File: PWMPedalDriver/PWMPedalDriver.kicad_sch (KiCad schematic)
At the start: 13 parts, among them U1 TLV172IDCK, U2 TLV172IDCK, U3 TLV172IDCK

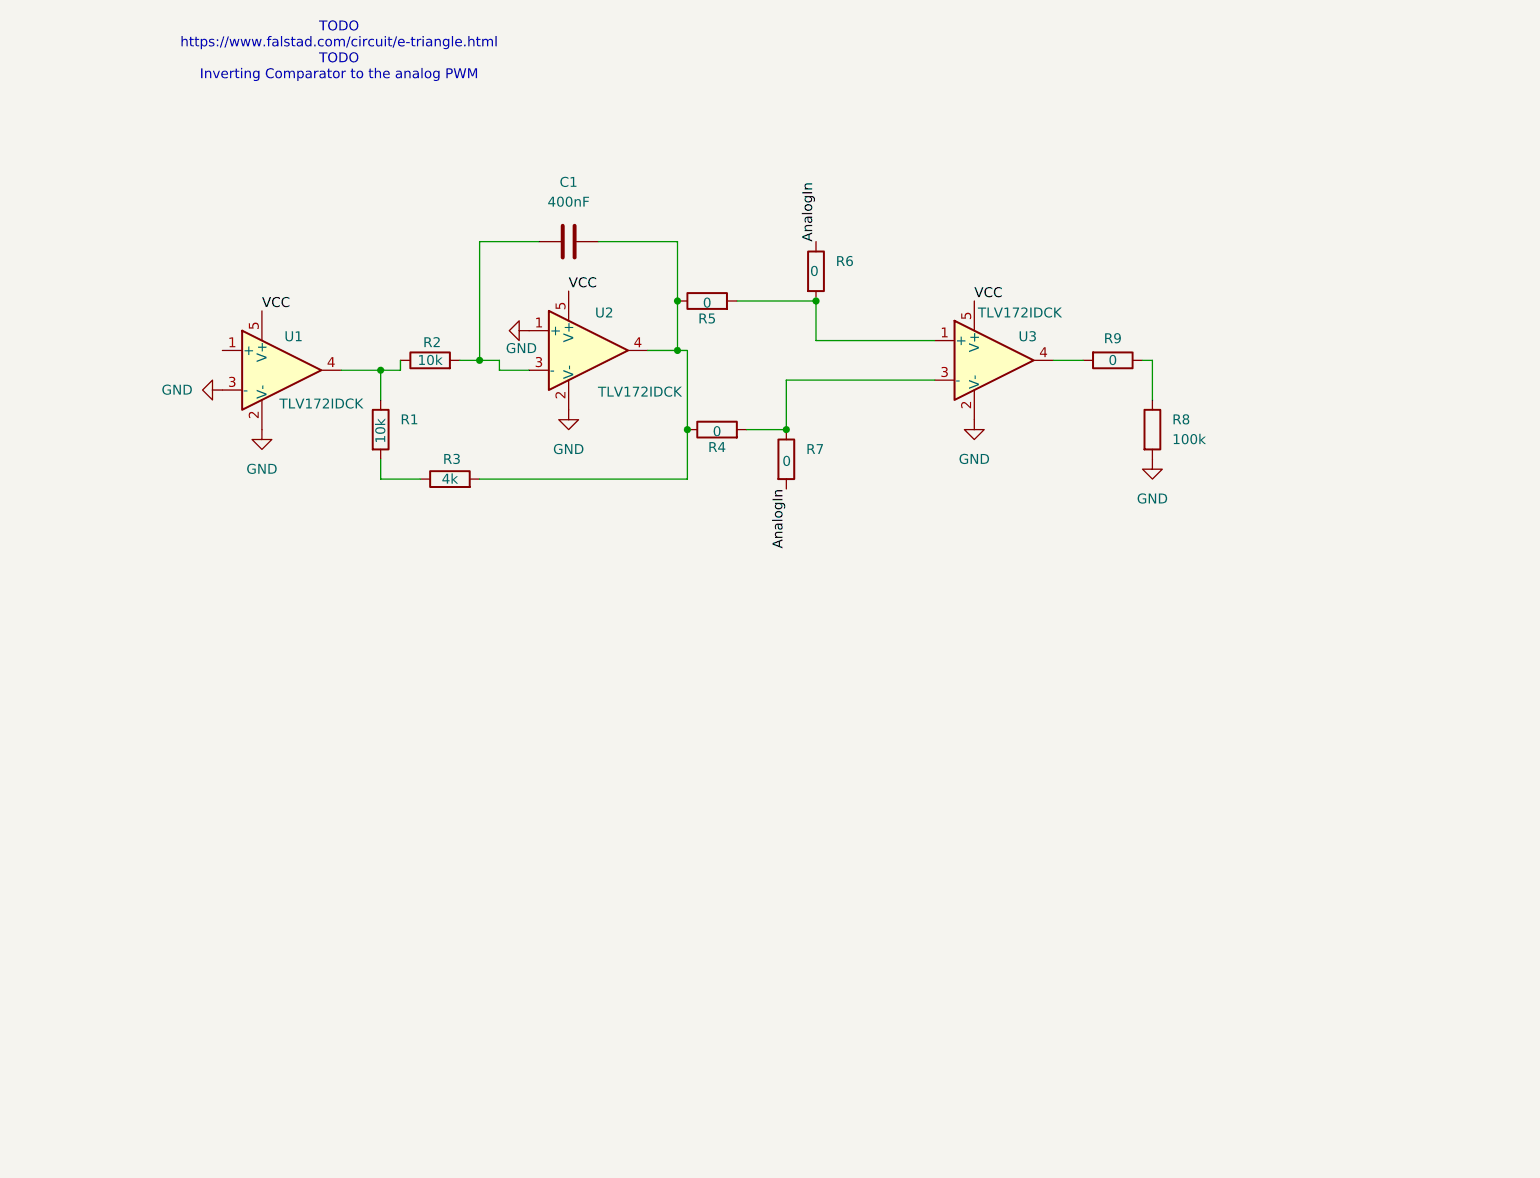
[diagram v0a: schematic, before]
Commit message: Simulated Triangle -> PWM Driver.
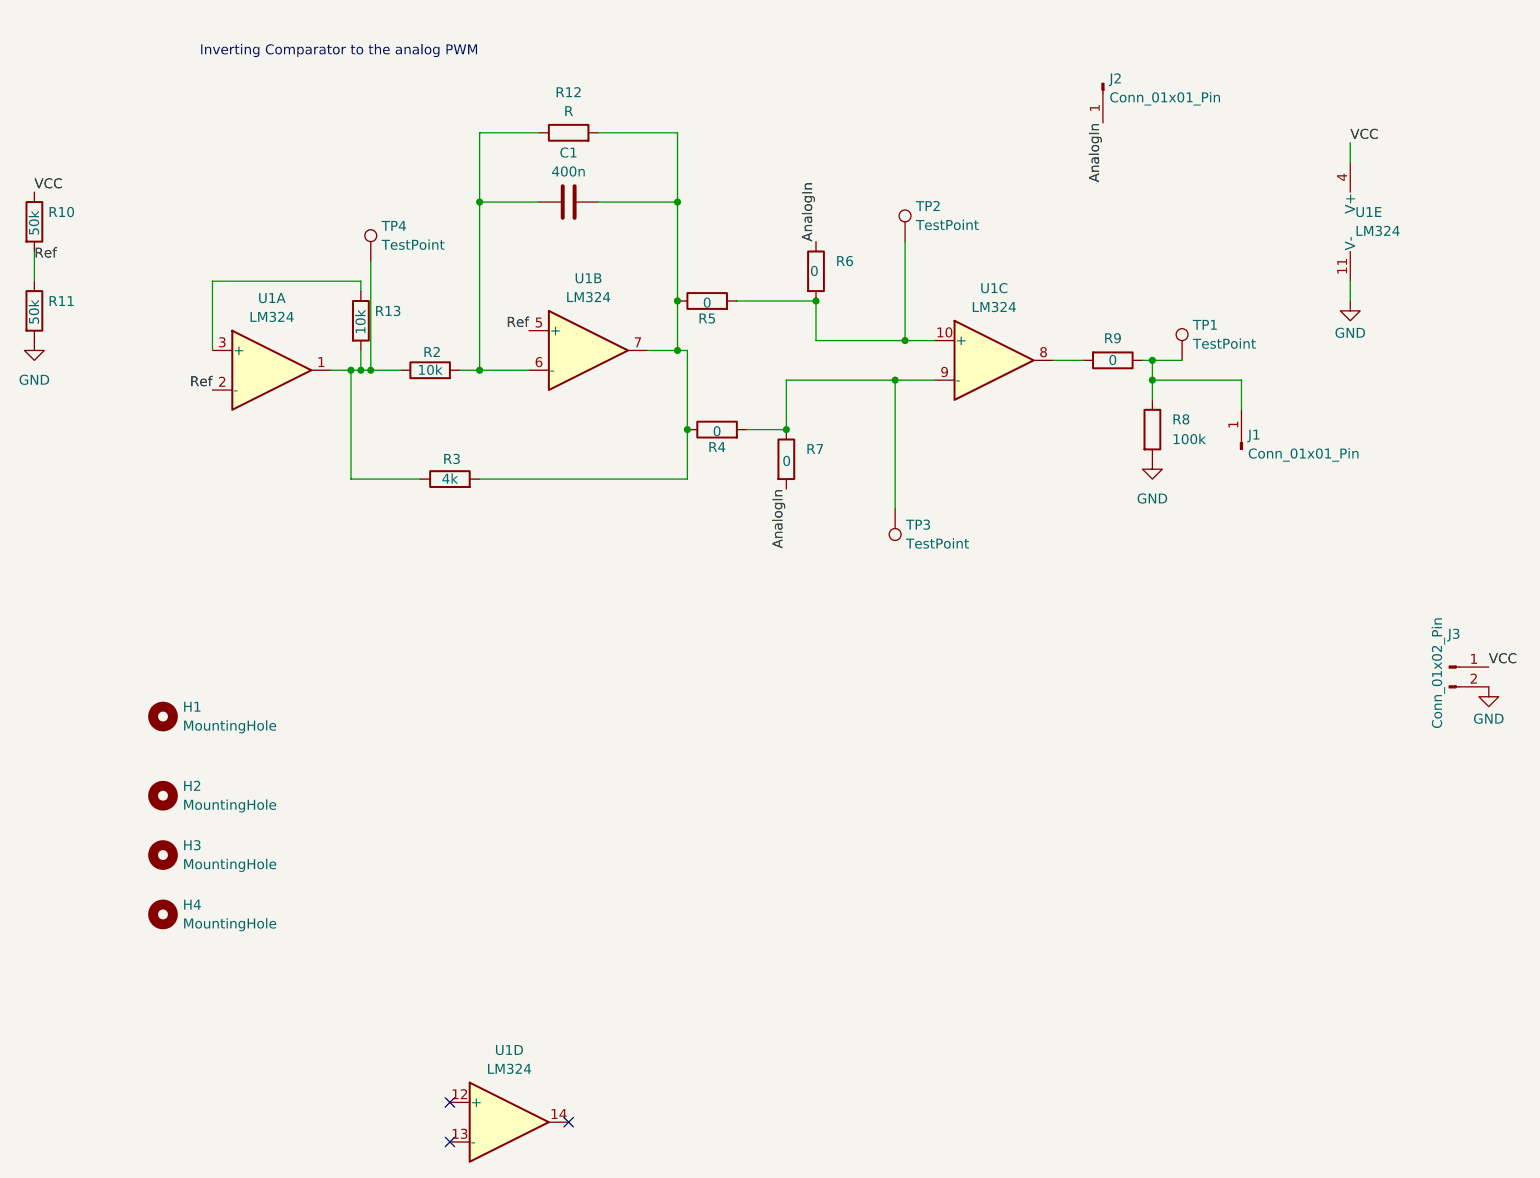
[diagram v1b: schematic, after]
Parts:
- removed R1: 10k, symbol Device:R
- removed U1, U2, U3: TLV172IDCK, Package_TO_SOT_SMD:SOT-353_SC-70-5, symbol Amplifier_Operational:TLV172IDCK
- added H1, H2, H3, H4: MountingHole, MountingHole:MountingHole_3.2mm_M3, symbol Mechanical:MountingHole
- added J1, J2: Conn_01x01_Pin, Connector_PinHeader_2.54mm:PinHeader_1x01_P2.54mm_Vertical, symbol Connector:Conn_01x01_Pin
- added J3: Conn_01x02_Pin, Connector_PinHeader_2.54mm:PinHeader_1x02_P2.54mm_Vertical, symbol Connector:Conn_01x02_Pin
- added R10, R11: 50k, Resistor_SMD:R_0402_1005Metric_Pad0.72x0.64mm_HandSolder, symbol Device:R
- added R12: R, Resistor_SMD:R_0402_1005Metric_Pad0.72x0.64mm_HandSolder, symbol Device:R
- added R13: 10k, Resistor_SMD:R_0402_1005Metric_Pad0.72x0.64mm_HandSolder, symbol Device:R
- added TP1, TP2, TP3, TP4: TestPoint, TestPoint:TestPoint_Loop_D2.60mm_Drill1.4mm_Beaded, symbol Connector:TestPoint
- added U1: LM324, Package_SO:SOIC-14_3.9x8.7mm_P1.27mm, symbol Amplifier_Operational:LM324
- C1: value 400nF -> 400n; footprint (none) -> Capacitor_SMD:C_0402_1005Metric_Pad0.74x0.62mm_HandSolder
- R2, R3, R4, R5, R6, R7, R8, R9: footprint (none) -> Resistor_SMD:R_0402_1005Metric_Pad0.72x0.64mm_HandSolder
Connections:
- net AnalogIn: now also J2.1 (Pin_1)
- net GND: now also J3.2 (Pin_2), R11.2, U1.11 (V-)
- net VCC: now also J3.1 (Pin_1), R10.1, U1.4 (V+)
- net at R2.1: now also R3.1, R13.2, TP4.1, U1.1
- net at C1.2, R3.2, R4.1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: now also R12.2, U1.7
- net at R4.2, R7.1: now also TP3.1, U1.9 (-)
- net at R5.2, R6.2: now also TP2.1, U1.10 (+)
- net at C1.1, R2.2: now also R12.1, U1.6 (-)
- net at R9.2: now also U1.8
- net at R8.1, R9.1: now also J1.1 (Pin_1), TP1.1
- new net: R13.1, U1.3 (+)
- new net Ref: R10.2, R11.1, U1.2 (-), U1.5 (+)
- no-connect marks 0 -> 3
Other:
- note added: "Inverting Comparator to the analog PWM"
- note removed: "TODO https://www.falstad.com/circuit/e-triangle.html TODO Inverting Comparator to the analog PWM"
- moved on the sheet: C1, R2

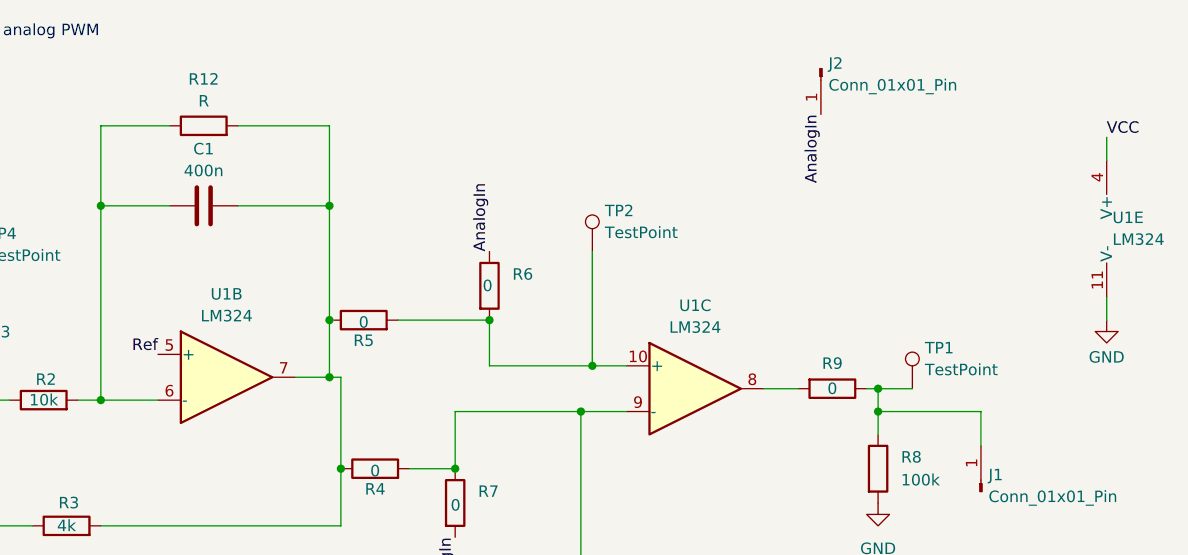
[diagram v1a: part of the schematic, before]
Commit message: First pass placement
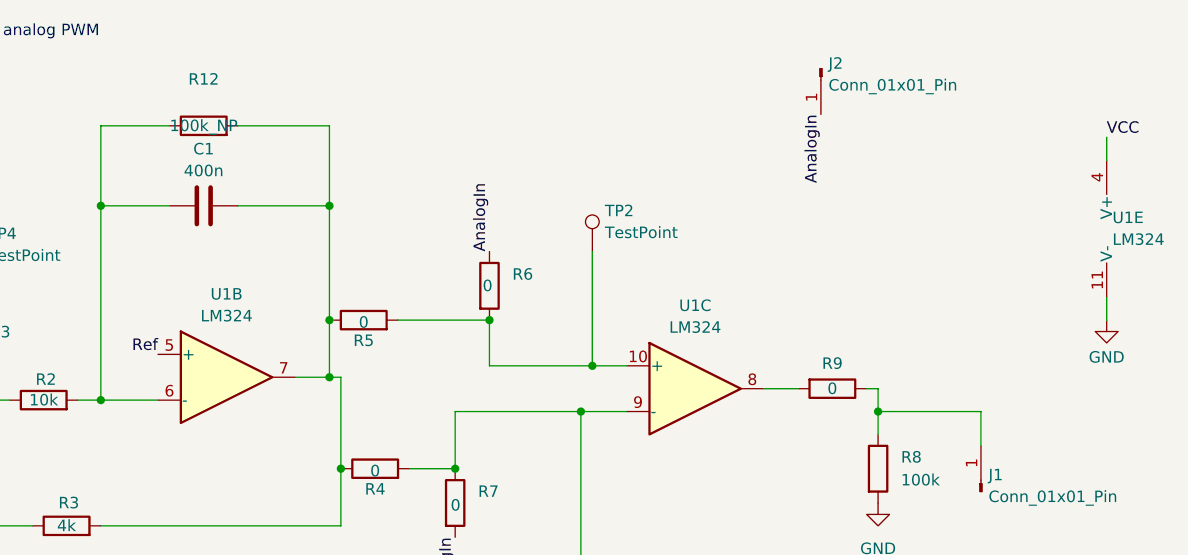
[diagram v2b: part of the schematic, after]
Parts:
- removed TP1: TestPoint, TestPoint:TestPoint_Loop_D2.60mm_Drill1.4mm_Beaded, symbol Connector:TestPoint
- R12: value R -> 100k_NP
- TP2, TP3, TP4: footprint TestPoint:TestPoint_Loop_D2.60mm_Drill1.4mm_Beaded -> TestPoint:TestPoint_Loop_D2.60mm_Drill0.9mm_Beaded
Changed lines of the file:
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@@
-	)
-	(junction
-		(at 227.33 60.96)
-		(diameter 0)
-		(color 0 0 0 0)
 	)
 	(junction
@@
 		(pts
 			(xy 227.33 60.96) (xy 227.33 63.5)
-		)
-		(stroke
-			(width 0)
-			(type default)
-		)
-	)
-	(wire
-		(pts
-			(xy 227.33 60.96) (xy 231.14 60.96)
 		)
 		(stroke
@@
 			)
 		)
-		(property "Footprint" "TestPoint:TestPoint_Loop_D2.60mm_Drill1.4mm_Beaded"
+		(property "Footprint" "TestPoint:TestPoint_Loop_D2.60mm_Drill0.9mm_Beaded"
 			(at 200.66 45.72 0)
 			(effects
@@
 		(on_board yes)
 		(dnp no)
-		(fields_autoplaced yes)
 		(property "Reference" "R12"
 			(at 152.4 26.5895 90)
@@
 			)
 		)
-		(property "Value" "R"
-			(at 152.4 29.0138 90)
+		(property "Value" "100k_NP"
+			(at 152.4 31.75 90)
 			(effects
 				(font
@@
 			)
 		)
-		(property "Footprint" "TestPoint:TestPoint_Loop_D2.60mm_Drill1.4mm_Beaded"
+		(property "Footprint" "TestPoint:TestPoint_Loop_D2.60mm_Drill0.9mm_Beaded"
 			(at 132.08 48.26 0)
 			(effects
@@
 	(symbol
 		(lib_id "Connector:TestPoint")
-		(at 231.14 60.96 0)
-		(unit 1)
-		(exclude_from_sim no)
-		(in_bom yes)
-		(on_board yes)
-		(dnp no)
-		(fields_autoplaced yes)
-		(property "Reference" "TP1"
-			(at 232.537 56.4458 0)
-			(effects
-				(font
-					(size 1.27 1.27)
-				)
-				(justify left)
-			)
-		)
-		(property "Value" "TestPoint"
-			(at 232.537 58.8701 0)
-			(effects
-				(font
-					(size 1.27 1.27)
-				)
-				(justify left)
-			)
-		)
-		(property "Footprint" "TestPoint:TestPoint_Loop_D2.60mm_Drill1.4mm_Beaded"
-			(at 236.22 60.96 0)
-			(effects
-				(font
-					(size 1.27 1.27)
-				)
-				(hide yes)
-			)
-		)
-		(property "Datasheet" "~"
-			(at 236.22 60.96 0)
-			(effects
-				(font
-					(size 1.27 1.27)
-				)
-				(hide yes)
-			)
-		)
-		(property "Description" "test point"
-			(at 231.14 60.96 0)
-			(effects
-				(font
-					(size 1.27 1.27)
-				)
-				(hide yes)
-			)
-		)
-		(pin "1"
-		)
-		(instances
-			(project ""
-				(path "/ca3f4581-2760-476b-ae38-fbfd5da505cf"
-					(reference "TP1")
-					(unit 1)
-				)
-			)
-		)
-	)
-	(symbol
-		(lib_id "Connector:TestPoint")
 		(at 194.31 80.01 180)
 		(unit 1)
@@
 			)
 		)
-		(property "Footprint" "TestPoint:TestPoint_Loop_D2.60mm_Drill1.4mm_Beaded"
+		(property "Footprint" "TestPoint:TestPoint_Loop_D2.60mm_Drill0.9mm_Beaded"
 			(at 189.23 80.01 0)
 			(effects

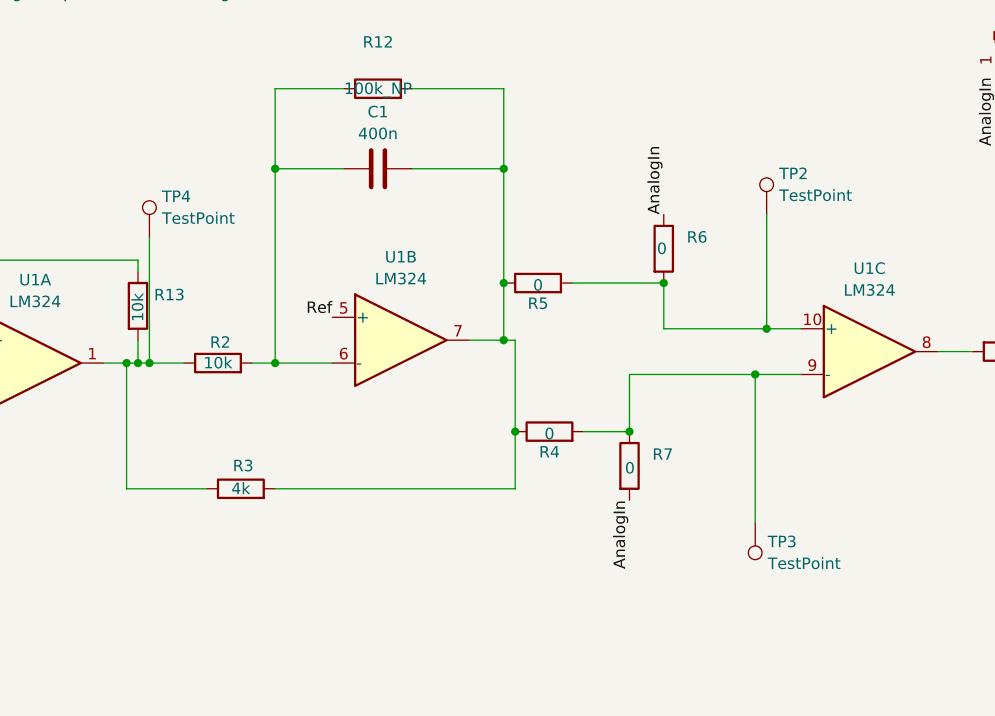
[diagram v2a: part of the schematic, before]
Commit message: Potential Routing / Placement for PWM
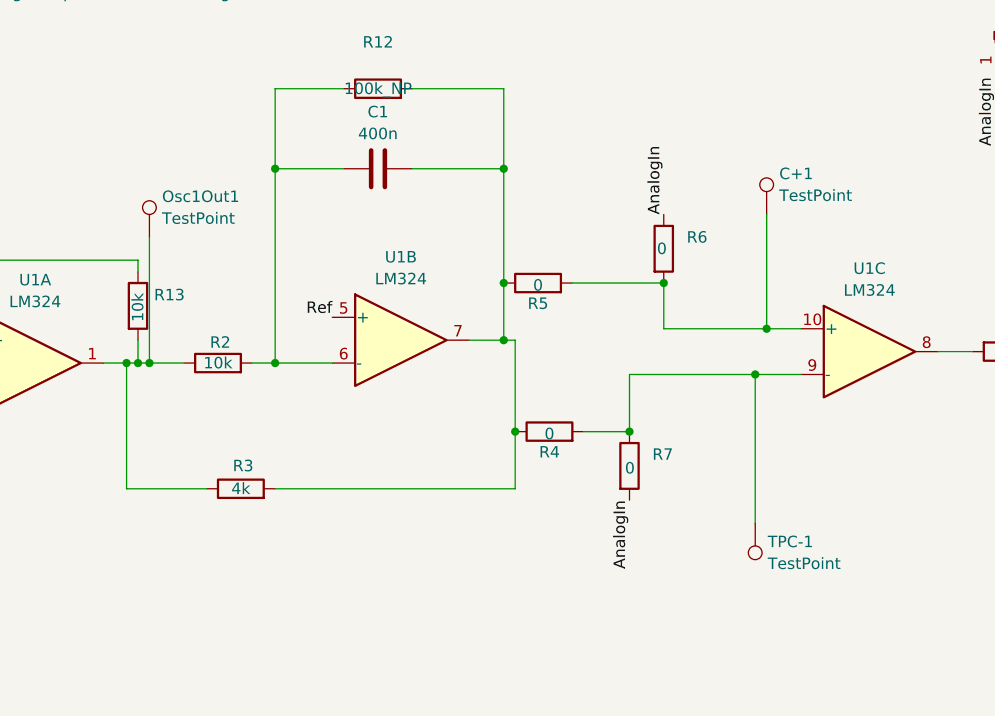
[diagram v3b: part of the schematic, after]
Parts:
- renumbered TP2 to C+1, TP4 to Osc1Out1, TP3 to TPC-1
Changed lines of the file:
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@@
 		(dnp no)
 		(fields_autoplaced yes)
-		(property "Reference" "TP2"
+		(property "Reference" "C+1"
 			(at 196.977 41.2058 0)
 			(effects
@@
 			(project "PWMPedalDriver"
 				(path "/ca3f4581-2760-476b-ae38-fbfd5da505cf"
-					(reference "TP2")
+					(reference "C+1")
 					(unit 1)
 				)
@@
 		(dnp no)
 		(fields_autoplaced yes)
-		(property "Reference" "TP4"
+		(property "Reference" "Osc1Out1"
 			(at 128.397 43.7458 0)
 			(effects
@@
 			(project "PWMPedalDriver"
 				(path "/ca3f4581-2760-476b-ae38-fbfd5da505cf"
-					(reference "TP4")
+					(reference "Osc1Out1")
 					(unit 1)
 				)
@@
 		(dnp no)
 		(fields_autoplaced yes)
-		(property "Reference" "TP3"
+		(property "Reference" "TPC-1"
 			(at 195.707 82.0998 0)
 			(effects
@@
 			(project "PWMPedalDriver"
 				(path "/ca3f4581-2760-476b-ae38-fbfd5da505cf"
-					(reference "TP3")
-					(unit 1)
-				)
+					(reference "TPC-1")
+					(unit 1)
+				)

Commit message: Shipped Board
Shipped out the Analog -> PWM driver
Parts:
- removed H1, H2: MountingHole, MountingHole:MountingHole_3.2mm_M3, symbol Mechanical:MountingHole
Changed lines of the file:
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@@
-	)
-	(symbol
-		(lib_id "Mechanical:MountingHole")
-		(at 100.33 116.84 0)
-		(unit 1)
-		(exclude_from_sim yes)
-		(in_bom no)
-		(on_board yes)
-		(dnp no)
-		(fields_autoplaced yes)
-		(property "Reference" "H2"
-			(at 102.87 115.6278 0)
-			(effects
-				(font
-					(size 1.27 1.27)
-				)
-				(justify left)
-			)
-		)
-		(property "Value" "MountingHole"
-			(at 102.87 118.0521 0)
-			(effects
-				(font
-					(size 1.27 1.27)
-				)
-				(justify left)
-			)
-		)
-		(property "Footprint" "MountingHole:MountingHole_3.2mm_M3"
-			(at 100.33 116.84 0)
-			(effects
-				(font
-					(size 1.27 1.27)
-				)
-				(hide yes)
-			)
-		)
-		(property "Datasheet" "~"
-			(at 100.33 116.84 0)
-			(effects
-				(font
-					(size 1.27 1.27)
-				)
-				(hide yes)
-			)
-		)
-		(property "Description" "Mounting Hole without connection"
-			(at 100.33 116.84 0)
-			(effects
-				(font
-					(size 1.27 1.27)
-				)
-				(hide yes)
-			)
-		)
-		(instances
-			(project "PWMPedalDriver"
-				(path "/ca3f4581-2760-476b-ae38-fbfd5da505cf"
-					(reference "H2")
-					(unit 1)
-				)
-			)
-		)
 	)
 	(symbol
@@
 					(unit 1)
 				)
-			)
-		)
-	)
-	(symbol
-		(lib_id "Mechanical:MountingHole")
-		(at 100.33 106.68 0)
-		(unit 1)
-		(exclude_from_sim yes)
-		(in_bom no)
-		(on_board yes)
-		(dnp no)
-		(fields_autoplaced yes)
-		(property "Reference" "H1"
-			(at 102.87 105.4678 0)
-			(effects
-				(font
-					(size 1.27 1.27)
-				)
-				(justify left)
-			)
-		)
-		(property "Value" "MountingHole"
-			(at 102.87 107.8921 0)
-			(effects
-				(font
-					(size 1.27 1.27)
-				)
-				(justify left)
-			)
-		)
-		(property "Footprint" "MountingHole:MountingHole_3.2mm_M3"
-			(at 100.33 106.68 0)
-			(effects
-				(font
-					(size 1.27 1.27)
-				)
-				(hide yes)
-			)
-		)
-		(property "Datasheet" "~"
-			(at 100.33 106.68 0)
-			(effects
-				(font
-					(size 1.27 1.27)
-				)
-				(hide yes)
-			)
-		)
-		(property "Description" "Mounting Hole without connection"
-			(at 100.33 106.68 0)
-			(effects
-				(font
-					(size 1.27 1.27)
-				)
-				(hide yes)
-			)
-		)
-		(instances
-			(project ""
-				(path "/ca3f4581-2760-476b-ae38-fbfd5da505cf"
-					(reference "H1")
-					(unit 1)
-				)
